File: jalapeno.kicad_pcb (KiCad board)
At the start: 2 copper layers, 252.4 x 81 mm, 120 parts, among them IC1 ATMEGA32U4-AU, J1 USB_B, K1 esc, K10 o, K11 p, K12 back, K12_1 KEYSW, K13 tab, K14 a, K15 s, K16 d, K17 f, K18 g, K19 h, K2 q, K20 j, K21 k, K22 l, K23 ;, K24 \, K25 caps, K26 z, K27 x, K28 c, K29 v, K3 w, K30 b, K31 n, K32 m, K33 ,, K34 ., K35 enter, K35_1 KEYSW, K36 ctrl, K37 gui, K38 alt, K39 space, K39_1 KEYSW, K4 e, K40 alt, K40_1 KEYSW, K41 gui, K41_1 KEYSW, K42 ctrl, K43 KEYSW, K44 KEYSW, K5 r, K6 t, K7 y, K8 u, K9 i, SW1 SW_PUSH, U1 MDBT40, U2 SPX3819M5-L-3-3, U3 MCP73831T-2ACI/OT, Y1 XTAL_GND

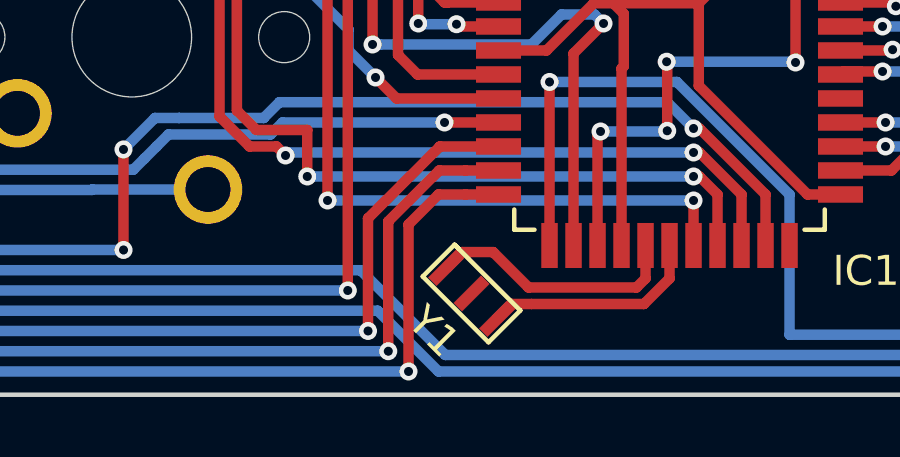
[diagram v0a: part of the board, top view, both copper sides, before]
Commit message: update crystal footprint + regenerated new netlist
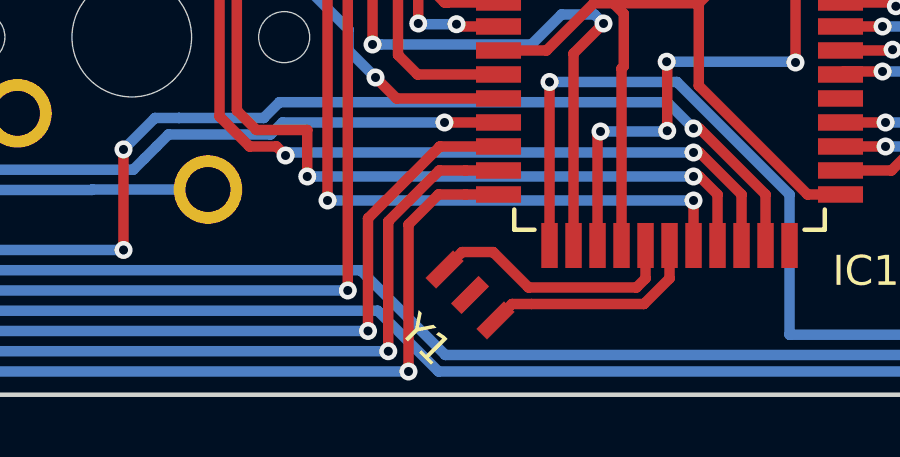
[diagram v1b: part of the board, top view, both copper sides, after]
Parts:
- removed LOGO: , logo:LOGO_small
- JST1: footprint kicad-libraries-master:JST-PH-2 -> kicad-libraries:JST-PH-2
- K12_1, K35_1, K41_1, K43: footprint finn:CHERRY_PCB_100H_NO_BORDER -> Jalapeno:CHERRY_PCB_100H_NO_BORDER
- K39: footprint finn:CHERRY_PCB_625H -> Jalapeno:CHERRY_PCB_625H
- K40_1, K44: footprint finn:CHERRY_PCB_125H_NO_BORDER -> Jalapeno:CHERRY_PCB_125H_NO_BORDER
- U1: footprint Rf_Modules_alt:MDBT40 -> RF_Modules_Custom:MDBT40
- Y1: footprint finn:resonator-smd3-3.2x1.3mm -> Jalapeno:smd_resonator_3pin_3x1.2mm
- moved Y1 0.07 mm to (166.1, 101.5)
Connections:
- Y1 pad 1: Net-(IC1-Pad17) -> Net-(IC1-Pad16)
- Y1 pad 2: Net-(IC1-Pad16) -> Net-(IC1-Pad17)

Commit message: added new footprints
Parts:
- added J2: AVR-ISP-6, Jalapeno:AVR_ICSP_3x2_NO_SILK, F.Cu at (267.7, 65.6)
- added J3: Conn_01x04, Jalapeno:AVR_2x2_NO_SILK, F.Cu at (22.9, 64.3)
- added R10: 10k, Resistors_SMD:R_0805_HandSoldering, F.Cu at (183.9, 87.2)
- added R9: 10k, Resistors_SMD:R_0805_HandSoldering, F.Cu at (47.5, 50.9)
- added T1: Conn_01x01, testpoint:TestPoint_Pad_1.0x1.0mm, F.Cu at (109.3, 102.6)
- added T2: Conn_01x01, testpoint:TestPoint_Pad_1.0x1.0mm, F.Cu at (109.3, 100.9)
- R4, R5: value 22 -> 22ohm
- U1: footprint RF_Modules_Custom:MDBT40 -> Jalapeno:MDBT40
- moved C1 2.35 mm to (183.9, 85.1)
- moved SW1 1.65 mm to (47.5, 56.6)
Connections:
- net Net-(IC1-Pad13) renamed /RESET
- IC1 pad 27: Net-(IC1-Pad27) -> COL_10
- IC1 pad 33: +3V3 -> Net-(IC1-Pad33)
- IC1 pad 8: COL_10 -> Net-(IC1-Pad8)
- U1 pad 36: Net-(U1-Pad36) -> /SWDCLK
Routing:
- net ROW_1: track 314.9 -> 0.00 mm, vias 19 -> 0
- net ROW_4: track 308.7 -> 0.00 mm, vias 9 -> 0
- net ROW_2: track 301.6 -> 0.00 mm, vias 17 -> 0
- net COL_7: track 298.9 -> 0.00 mm, vias 10 -> 0
- net COL_12: track 273.4 -> 0.00 mm, vias 10 -> 0
- net ROW_3: track 266.7 -> 0.00 mm, vias 15 -> 0
- net VBUS: track 257.6 -> 0.00 mm, vias 19 -> 0
- net COL_8: track 233.7 -> 0.00 mm, vias 10 -> 0
- net COL_6: track 226.7 -> 0.00 mm, vias 8 -> 0
- net +3V3: track 212.0 -> 0.00 mm, vias 18 -> 0
- net COL_9: track 210.2 -> 0.00 mm, vias 8 -> 0
- net Net-(R1-Pad2): track 208.6 -> 0.00 mm, vias 4 -> 0
- net COL_11: track 201.7 -> 0.00 mm, vias 6 -> 0
- net COL_5: track 201.5 -> 0.00 mm, vias 6 -> 0
- net COL_1: track 194.5 -> 0.00 mm, vias 8 -> 0
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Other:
- board text added: "BL factory reset"
- board text removed: "Jalapeno BLE A staggered 40% bluetooth keyboard v0.0.1 - CC Attribution-NonCommercial 4.0"

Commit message: started re-routing
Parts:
- moved C1 24.9 mm to (183.6, 110.0)
- moved R10 24.7 mm to (183.4, 112.0)
- moved C4 23.7 mm to (160.7, 108.4)
- moved C2 21.0 mm to (131.0, 108.6)
- moved Y1 11.2 mm to (173.8, 109.6), turned to 45 degrees
- moved R5 5.32 mm to (182.3, 46.5), turned to 270 degrees
- moved IC1 3.58 mm to (176.0, 92.7)
- moved R4 1.92 mm to (184.4, 47.3), turned to 270 degrees
- moved DB1 1.70 mm to (156.1, 42.1)
- moved R8 1.04 mm to (242.8, 58.8)
- moved C3 1.04 mm to (242.9, 51.4), turned to 0 degrees
- moved C6 0.81 mm to (241.8, 78.5)
- moved C7 0.81 mm to (237.3, 78.5)
- moved C5 0.81 mm to (239.6, 78.5)
- moved D38 0.10 mm to (209.9, 88.6)
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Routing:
- net ROW_2: track 0.00 -> 231.8 mm, vias 0 -> 12
- net ROW_1: track 0.00 -> 228.7 mm, vias 0 -> 12
- net ROW_3: track 0.00 -> 224.0 mm, vias 0 -> 12
- net VBUS: track 0.00 -> 212.1 mm, vias 0 -> 7
- net +BATT: track 0.00 -> 112.1 mm, vias 0 -> 4
- net ROW_4: track 0.00 -> 87.6 mm, vias 0 -> 6
- net Net-(J1-Pad3): track 0.00 -> 83.2 mm, vias 0 -> 2
- net Net-(J1-Pad2): track 0.00 -> 81.9 mm, vias 0 -> 2
- net +3V3: track 0.00 -> 78.9 mm, vias 0 -> 4
- net GND: track 0.00 -> 19.6 mm, vias 0 -> 9
- net Net-(D12-Pad2): track 0.00 -> 17.4 mm
- net Net-(D44-Pad2): track 0.00 -> 14.3 mm
- net Net-(D35-Pad2): track 0.00 -> 11.9 mm
- net /BATT_LVL: track 0.00 -> 11.5 mm, vias 0 -> 2
- net Net-(D18-Pad2): track 0.00 -> 7.78 mm
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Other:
- board text removed: "ble"

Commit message: new pcb & routing
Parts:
- removed D43, D44: D, Diodes_SMD:D_0805
- removed K12_1, K35_1, K41_1, K43: KEYSW, Jalapeno:CHERRY_PCB_100H_NO_BORDER
- removed K40_1, K44: KEYSW, Jalapeno:CHERRY_PCB_125H_NO_BORDER
- removed T1, T2: Conn_01x01, testpoint:TestPoint_Pad_1.0x1.0mm
- added K33_1: ,, Keyboard:CHERRY_PCB_100H, F.Cu at (228.6, 71.4)
- added K34_1: ., Keyboard:CHERRY_PCB_125H, F.Cu at (250.0, 71.4)
- added K37_1: alt, Keyboard:CHERRY_PCB_125H, F.Cu at (88.1, 90.5)
- added K38_1: space, Keyboard:CHERRY_PCB_225H, F.Cu at (121.4, 90.5)
- added LED1: WS2812B, WS2812B:WS2812B, B.Cu at (71.4, 81.0)
- added LED2: WS2812B, WS2812B:WS2812B, B.Cu at (123.8, 81.0)
- added LED3: WS2812B, WS2812B:WS2812B, B.Cu at (171.4, 81.0)
- added LED4: WS2812B, WS2812B:WS2812B, B.Cu at (223.8, 81.0)
- added LED5: WS2812B, WS2812B:WS2812B, B.Cu at (223.8, 42.9)
- added LED6: WS2812B, WS2812B:WS2812B, B.Cu at (171.4, 42.9)
- added LED7: WS2812B, WS2812B:WS2812B, B.Cu at (123.8, 42.9)
- added LED8: WS2812B, WS2812B:WS2812B, B.Cu at (71.4, 42.9)
- C1, C2, C3, C4, C5, C6, C7, D1, D10, D11, D12, D13, D14, D15, D16, D17, D18, D19, D2, D20, D21, D22, D23, D24, D25, D26, D27, D28, D29, D3, D30, D31, D32, D33, D34, D35, D36, D37, D38, D39, D4, D40, D41, D42, D5, D6, D7, D8, D9, DB1, IC1, J1, J2, J3, JST1, R1, R10, R2, R3, R4, R5, R6, R7, R8, R9, SW1, U1, U2, U3, Y1: moved to B.Cu
- K1, K10, K11, K14, K15, K16, K17, K18, K19, K2, K20, K21, K22, K26, K27, K28, K29, K3, K30, K31, K32, K34, K4, K5, K6, K7, K8, K9: moved to F.Cu
- K12: footprint Keyboard:CHERRY_PCB_200H -> Keyboard:CHERRY_PCB_100H; moved to F.Cu
- K13: footprint Keyboard:CHERRY_PCB_150H -> Keyboard:CHERRY_PCB_125H; moved to F.Cu
- K23: footprint Keyboard:CHERRY_PCB_100H -> Keyboard:CHERRY_PCB_175H; moved to F.Cu
- K24: value \ -> caps; footprint Keyboard:CHERRY_PCB_150H -> Keyboard:CHERRY_PCB_175H; moved to F.Cu
- K25: footprint Keyboard:CHERRY_PCB_175H -> Keyboard:CHERRY_PCB_100H; moved to F.Cu
- K33: footprint Keyboard:CHERRY_PCB_100H -> Keyboard:CHERRY_PCB_125H; moved to F.Cu
- K35: value enter -> ctrl; footprint Keyboard:CHERRY_PCB_225H -> Keyboard:CHERRY_PCB_125H; moved to F.Cu
- K36: value ctrl -> gui; footprint Keyboard:CHERRY_PCB_125H -> Keyboard:CHERRY_PCB_100H; moved to F.Cu
- K37: value gui -> alt; moved to F.Cu
- K38: value alt -> space; footprint Keyboard:CHERRY_PCB_125H -> Keyboard:CHERRY_PCB_625H; moved to F.Cu
- K39: value space -> alt; footprint Jalapeno:CHERRY_PCB_625H -> Keyboard:CHERRY_PCB_125H; moved to F.Cu
- K39_1: value KEYSW -> gui; footprint Keyboard:CHERRY_PCB_625H -> Keyboard:CHERRY_PCB_100H; moved to F.Cu
- K40: value alt -> gui; moved to F.Cu
- K41: value gui -> ctrl; footprint Keyboard:CHERRY_PCB_100H -> Keyboard:CHERRY_PCB_125H; moved to F.Cu
- K42: value ctrl -> KEYSW; footprint Keyboard:CHERRY_PCB_125H -> Keyboard:CHERRY_PCB_275H; moved to F.Cu
- LED1_0, LED2_0: footprint LEDs:LED_D1.8mm_W1.8mm_H2.4mm_Horizontal_O1.27mm_Z1.6mm -> LEDs:LED_0805_HandSoldering; moved to B.Cu
- moved J3 238.7 mm to (261.7, 61.9), turned to 180 degrees
- moved J2 234.2 mm to (33.5, 61.9), turned to 270 degrees
- moved K1 216.7 mm to (42.9, 33.3)
- moved D1 212.6 mm to (42.9, 38.7)
- moved K12 211.9 mm to (252.4, 33.3)
- moved K13 209.6 mm to (45.2, 52.4)
- moved D12 207.0 mm to (252.4, 38.7)
- moved D13 205.2 mm to (45.2, 57.7)
- moved K36 190.5 mm to (66.7, 90.5)
- moved D23 190.3 mm to (245.3, 57.7)
- moved D36 186.3 mm to (66.7, 95.8)
- moved K23 185.8 mm to (245.3, 52.4)
- moved D40 183.2 mm to (250.0, 95.8)
- moved D34 182.0 mm to (251.2, 76.8)
- moved K34 178.6 mm to (252.4, 71.4)
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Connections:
- D24 pad 1: ROW_2 -> ROW_3
- D35 pad 1: ROW_3 -> ROW_4
- IC1 pad 22: Net-(IC1-Pad22) -> RGB
- J1 pad 4: GND -> Net-(J1-Pad4)
- J1 pad 5: Net-(J1-Pad5) -> GND
- J1 pad 6: (no net) -> Net-(J1-Pad6)
- K24 pad 1: COL_12 -> COL_1
- K25 pad 1: COL_1 -> COL_2
- K26 pad 1: COL_2 -> COL_3
- K27 pad 1: COL_3 -> COL_4
- K28 pad 1: COL_4 -> COL_5
- K29 pad 1: COL_5 -> COL_6
- K30 pad 1: COL_6 -> COL_7
- K31 pad 1: COL_7 -> COL_8
- K32 pad 1: COL_8 -> COL_9
- K33 pad 1: COL_9 -> COL_10
- K34 pad 1: COL_10 -> COL_11
- K35 pad 1: COL_11 -> COL_1
- K36 pad 1: COL_1 -> COL_2
- K37 pad 1: COL_2 -> COL_3
- K38 pad 1: COL_3 -> COL_4
- K39 pad 1: COL_4 -> COL_5
- K39_1 pad 1: COL_4 -> COL_5
- K40 pad 1: COL_5 -> COL_6
- K41 pad 1: COL_6 -> COL_7
- K42 pad 1: COL_7 -> COL_8
- U1 pad 24: /DFU -> Net-(U1-Pad24)
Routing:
- net +3V3: track 78.9 -> 456.6 mm, vias 4 -> 14
- net ROW_4: track 87.6 -> 274.1 mm, vias 6 -> 17
- net VBUS: track 212.1 -> 381.9 mm, vias 7 -> 13
- net RGB: track 0.00 -> 124.7 mm, vias 0 -> 4
- net Net-(R2-Pad1): track 0.00 -> 109.7 mm, vias 0 -> 2
- net Net-(J1-Pad3): track 83.2 -> 6.58 mm, vias 2 -> 0
- net Net-(J1-Pad2): track 81.9 -> 6.25 mm, vias 2 -> 0
- net Net-(LED4-Pad2): track 0.00 -> 61.4 mm, vias 0 -> 4
- net /BATT_LVL: track 11.5 -> 68.8 mm
- net Net-(IC1-Pad4): track 0.00 -> 53.7 mm
- net Net-(IC1-Pad3): track 0.00 -> 53.6 mm
- net Net-(LED5-Pad2): track 0.00 -> 50.9 mm, vias 0 -> 2
- net Net-(LED1-Pad2): track 0.00 -> 50.4 mm, vias 0 -> 2
- net Net-(LED7-Pad2): track 0.00 -> 50.4 mm, vias 0 -> 2
- net /AREF: track 0.00 -> 49.5 mm, vias 0 -> 2
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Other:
- board size 252.4 x 81 mm -> 233.4 x 81 mm
- net class Default: trace_width 0.35 -> 0.16
- rule trace_min: 0.35 -> 0.15
- board text removed: "+"
- board text removed: "-"
- board text removed: "BL factory reset"

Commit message: finished routing...
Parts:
- added H1: MountingHole_2.2mm_M2_Pad, Mounting_Holes:MountingHole_2.2mm_M2_Pad, F.Cu at (242.9, 42.9)
- added H2: MountingHole_2.2mm_M2_Pad, Mounting_Holes:MountingHole_2.2mm_M2_Pad, F.Cu at (147.6, 42.9)
- added H3: MountingHole_2.2mm_M2_Pad, Mounting_Holes:MountingHole_2.2mm_M2_Pad, F.Cu at (52.4, 42.9)
- added H4: MountingHole_2.2mm_M2_Pad, Mounting_Holes:MountingHole_2.2mm_M2_Pad, F.Cu at (52.4, 81.0)
- added H5: MountingHole_2.2mm_M2_Pad, Mounting_Holes:MountingHole_2.2mm_M2_Pad, F.Cu at (147.6, 81.0)
- added H6: MountingHole_2.2mm_M2_Pad, Mounting_Holes:MountingHole_2.2mm_M2_Pad, F.Cu at (242.9, 81.0)
- moved C4 3.77 mm to (152.5, 83.8)
- moved Y1 0.91 mm to (146.5, 96.8)
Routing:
- net /MOSI: track 0.00 -> 233.2 mm, vias 0 -> 6
- net /MISO: track 0.00 -> 229.5 mm, vias 0 -> 8
- net /RESET: track 2.90 -> 232.1 mm, vias 0 -> 4
- net /SCK: track 0.00 -> 228.3 mm, vias 0 -> 4
- net COL_5: track 0.00 -> 218.1 mm, vias 0 -> 8
- net COL_6: track 0.00 -> 209.4 mm, vias 0 -> 8
- net COL_10: track 0.00 -> 204.3 mm, vias 0 -> 4
- net COL_11: track 0.00 -> 197.6 mm, vias 0 -> 5
- net COL_9: track 0.00 -> 188.9 mm, vias 0 -> 6
- net COL_12: track 0.00 -> 188.1 mm, vias 0 -> 4
- net COL_7: track 0.00 -> 182.5 mm, vias 0 -> 10
- net /4_SWDIO/RST: track 0.00 -> 172.5 mm, vias 0 -> 7
- net COL_1: track 0.00 -> 169.7 mm, vias 0 -> 10
- net COL_2: track 0.00 -> 159.1 mm, vias 0 -> 9
- net COL_4: track 0.00 -> 143.1 mm, vias 0 -> 6
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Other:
- net class Default: clearance 0.2 -> 0.15; trace_width 0.16 -> 0.15
- rule trace_clearance: 0.2 -> 0.15

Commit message: new routing
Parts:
- moved J2 228.2 mm to (261.7, 61.9), turned to 90 degrees
- moved J3 228.1 mm to (33.6, 61.9), turned to 0 degrees
- moved LED1_0 203.3 mm to (32.0, 76.0)
- moved LED2_0 202.0 mm to (32.0, 81.0)
- moved R2 200.8 mm to (34.0, 76.0), turned to 270 degrees
- moved R1 199.3 mm to (34.0, 81.0), turned to 90 degrees
- moved C3 80.9 mm to (209.6, 50.4), turned to 0 degrees
- moved C1 80.6 mm to (179.4, 88.4)
- moved U3 77.8 mm to (209.6, 46.5), turned to 90 degrees
- moved R8 74.9 mm to (209.6, 42.8), turned to 0 degrees
- moved R6 74.3 mm to (172.8, 97.6)
- moved R10 74.0 mm to (172.8, 95.6)
- moved Y1 52.6 mm to (198.6, 89.8), turned to 270 degrees
- moved IC1 50.3 mm to (190.2, 90.8), turned to 270 degrees
- moved U1 50.3 mm to (142.0, 93.4)
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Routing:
- net /MOSI: track 233.2 -> 0.00 mm, vias 6 -> 0
- net /MISO: track 229.5 -> 0.00 mm, vias 8 -> 0
- net /SCK: track 228.3 -> 0.00 mm, vias 4 -> 0
- net /RESET: track 232.1 -> 9.20 mm, vias 4 -> 0
- net COL_12: track 188.1 -> 0.00 mm, vias 4 -> 0
- net /4_SWDIO/RST: track 172.5 -> 0.00 mm, vias 7 -> 0
- net COL_10: track 204.3 -> 54.3 mm, vias 4 -> 2
- net ROW_4: track 361.3 -> 215.5 mm, vias 16 -> 8
- net COL_9: track 188.9 -> 51.8 mm, vias 6 -> 2
- net COL_11: track 197.6 -> 68.9 mm, vias 5 -> 2
- net RGB: track 114.3 -> 0.00 mm, vias 4 -> 0
- net Net-(R2-Pad1): track 108.7 -> 207.8 mm, vias 2 -> 4
- net Net-(R1-Pad2): track 72.3 -> 166.7 mm, vias 2 -> 6
- net /SWDCLK: track 93.7 -> 0.00 mm, vias 1 -> 0
- net COL_1: track 169.7 -> 77.3 mm, vias 10 -> 3
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
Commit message: new routing
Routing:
- net RGB: track 0.00 -> 190.0 mm, vias 0 -> 4
- net /RESET: track 9.20 -> 178.1 mm, vias 0 -> 2
- net COL_2: track 81.0 -> 241.1 mm, vias 3 -> 5
- net COL_8: track 83.3 -> 160.5 mm, vias 4 -> 8
- net COL_10: track 54.3 -> 124.8 mm, vias 2 -> 5
- net COL_9: track 51.8 -> 107.2 mm, vias 2 -> 4
- net COL_6: track 187.3 -> 233.9 mm, vias 5 -> 8
- net COL_4: track 127.4 -> 159.9 mm, vias 5 -> 6
- net COL_7: track 105.8 -> 128.7 mm, vias 4 -> 5
- net COL_5: track 179.4 -> 200.6 mm, vias 5 -> 6
- net COL_1: track 77.3 -> 91.2 mm, vias 3 -> 4
- net /BATT_LVL: track 112.8 -> 109.6 mm, vias 6 -> 7
- net COL_3: track 80.9 -> 84.0 mm

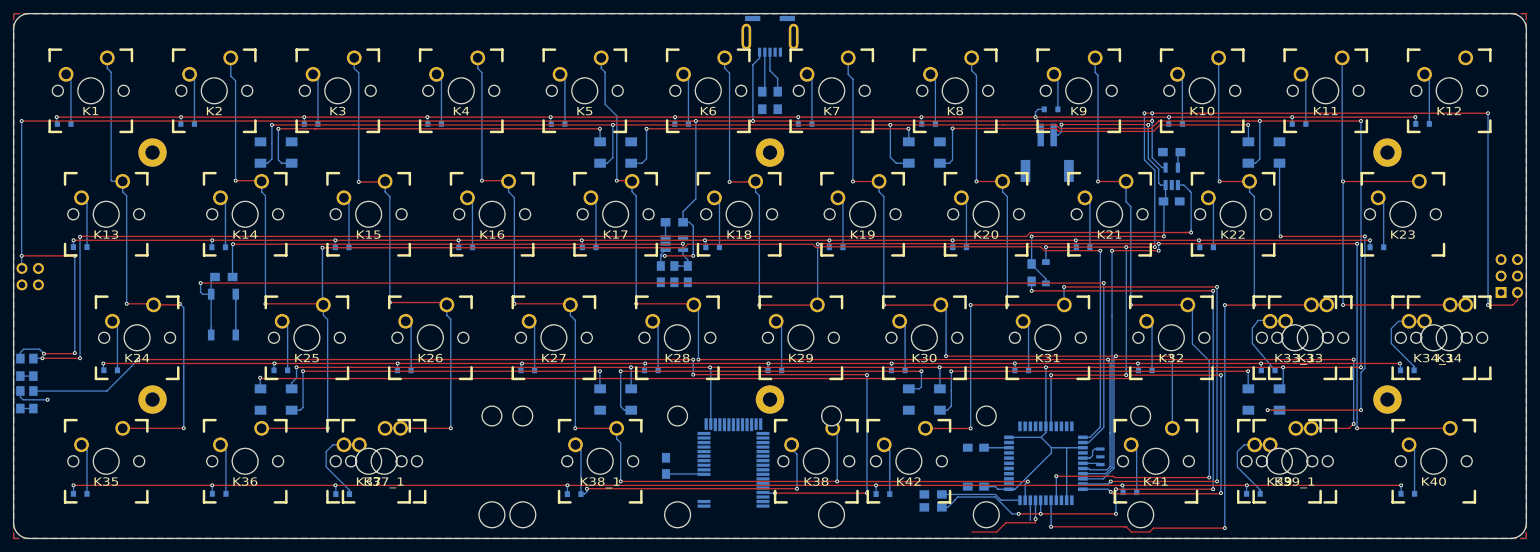
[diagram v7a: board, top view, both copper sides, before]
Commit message: new switch footprint
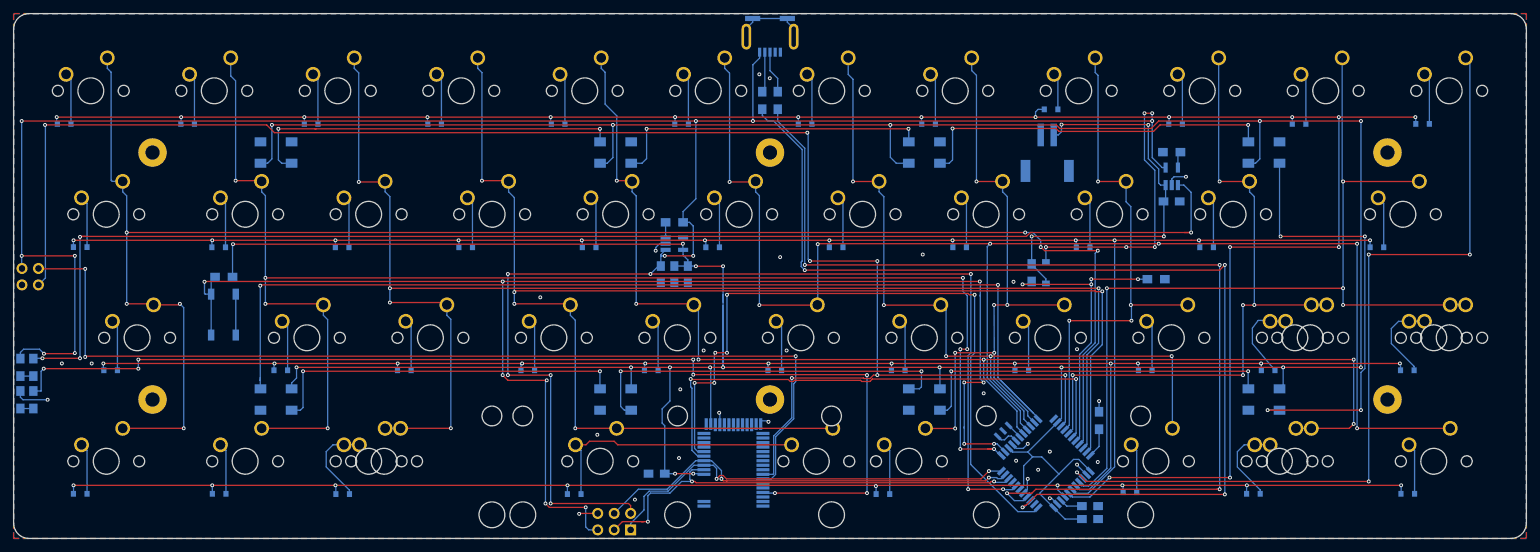
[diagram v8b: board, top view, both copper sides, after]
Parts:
- K1, K10, K11, K12, K14, K15, K16, K17, K18, K19, K2, K20, K21, K22, K25, K26, K27, K28, K29, K3, K30, K31, K32, K33_1, K34, K36, K37, K39_1, K4, K5, K6, K7, K8, K9: footprint Keyboard:CHERRY_PCB_100H -> Jalapeno:CHERRY_PCB_100H_NO_BORDER
- K13, K33, K34_1, K35, K37_1, K39, K40, K41: footprint Keyboard:CHERRY_PCB_125H -> Jalapeno:CHERRY_PCB_125H_NO_BORDER
- K23, K24: footprint Keyboard:CHERRY_PCB_175H -> Jalapeno:CHERRY_PCB_175H_NO_BORDER
- K38: footprint Keyboard:CHERRY_PCB_625H -> Jalapeno:CHERRY_PCB_625H_NO_BORDER
- K38_1: footprint Keyboard:CHERRY_PCB_225H -> Jalapeno:CHERRY_PCB_225H_NO_BORDER
- K42: footprint Keyboard:CHERRY_PCB_275H -> Jalapeno:CHERRY_PCB_275H_NO_BORDER
- moved J2 143.2 mm to (123.6, 99.8), turned to 180 degrees
- moved C4 65.9 mm to (197.0, 99.4), turned to 180 degrees
- moved C2 49.3 mm to (130.2, 92.4)
- moved R6 49.2 mm to (207.2, 62.4), turned to 180 degrees
- moved R10 28.0 mm to (198.4, 84.2), turned to 90 degrees
- moved C1 19.8 mm to (197.0, 97.4), turned to 0 degrees
- moved Y1 15.5 mm to (183.6, 85.8), turned to 45 degrees
- turned IC1 to 45 degrees
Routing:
- net /4_SWDIO/RST: track 0.00 -> 258.8 mm, vias 0 -> 7
- net COL_1: track 91.2 -> 260.0 mm, vias 4 -> 7
- net Net-(IC1-Pad3): track 0.00 -> 162.4 mm, vias 0 -> 4
- net Net-(IC1-Pad4): track 0.00 -> 161.2 mm, vias 0 -> 4
- net /SWDCLK: track 0.00 -> 151.7 mm, vias 0 -> 3
- net COL_3: track 84.0 -> 215.9 mm, vias 3 -> 5
- net COL_12: track 0.00 -> 128.4 mm, vias 0 -> 4
- net /7_BLE_IRQ: track 0.00 -> 108.1 mm, vias 0 -> 6
- net ROW_1: track 224.3 -> 323.2 mm, vias 12 -> 17
- net /8_BLE_CS: track 0.00 -> 81.8 mm, vias 0 -> 2
- net /SCK: track 0.00 -> 70.3 mm, vias 0 -> 3
- net COL_11: track 68.9 -> 138.7 mm, vias 2 -> 4
- net COL_4: track 159.9 -> 228.0 mm, vias 6 -> 5
- net /MOSI: track 0.00 -> 66.3 mm, vias 0 -> 2
- net /MISO: track 0.00 -> 65.9 mm, vias 0 -> 2
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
